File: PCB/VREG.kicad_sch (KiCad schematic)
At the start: 3 parts, among them U5 XC6220B331MR

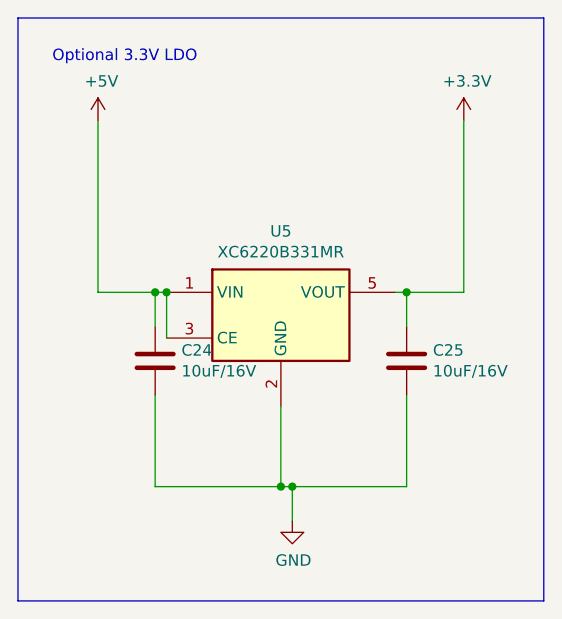
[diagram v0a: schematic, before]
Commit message: added .1uF for C2-C4
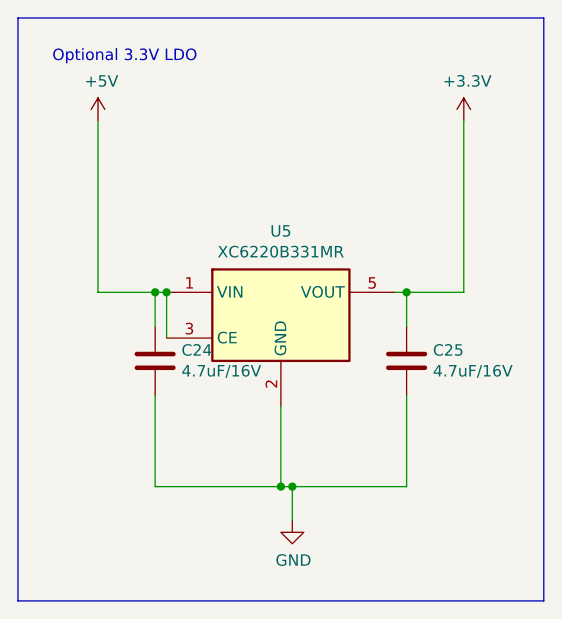
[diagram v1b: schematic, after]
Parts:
- C24, C25: value 10uF/16V -> 4.7uF/16V
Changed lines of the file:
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@@
       (effects (font (size 1.27 1.27)) (justify left))
     )
-    (property "Value" "10uF{slash}16V" (id 1) (at 179.451 98.933 0)
+    (property "Value" "4.7uF{slash}16V" (id 1) (at 179.451 98.933 0)
       (effects (font (size 1.27 1.27)) (justify left))
     )
@@
       (effects (font (size 1.27 1.27)) (justify left))
     )
-    (property "Value" "10uF{slash}16V" (id 1) (at 207.391 98.933 0)
+    (property "Value" "4.7uF{slash}16V" (id 1) (at 207.391 98.933 0)
       (effects (font (size 1.27 1.27)) (justify left))
     )

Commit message: fix(VREG): update C24,C25 value to 10uF to match DigiKey
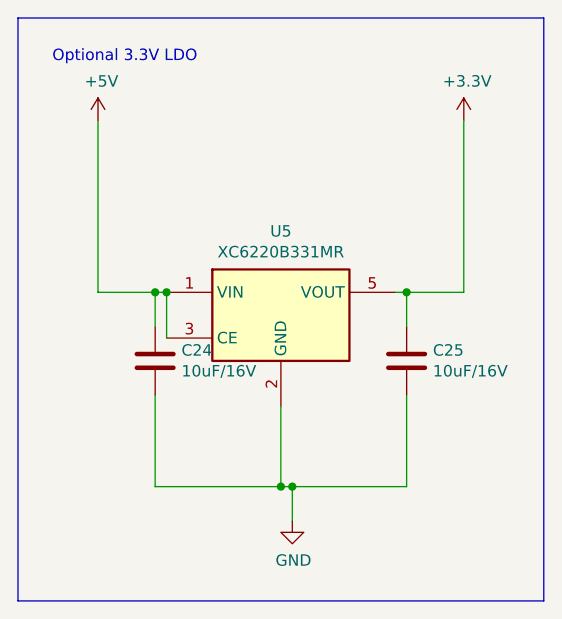
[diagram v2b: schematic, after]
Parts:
- C24, C25: value 4.7uF/16V -> 10uF/16V
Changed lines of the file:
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@@
       (effects (font (size 1.27 1.27)) (justify left))
     )
-    (property "Value" "4.7uF{slash}16V" (id 1) (at 179.451 98.933 0)
+    (property "Value" "10uF{slash}16V" (id 1) (at 179.451 98.933 0)
       (effects (font (size 1.27 1.27)) (justify left))
     )
@@
       (effects (font (size 1.27 1.27)) (justify left))
     )
-    (property "Value" "4.7uF{slash}16V" (id 1) (at 207.391 98.933 0)
+    (property "Value" "10uF{slash}16V" (id 1) (at 207.391 98.933 0)
       (effects (font (size 1.27 1.27)) (justify left))
     )
